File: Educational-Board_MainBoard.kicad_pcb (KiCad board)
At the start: 2 copper layers, 200 x 75 mm, 181 parts, among them J201 Screw_Terminal_01x02_P5mm, J202 USB-C_304A-ACP16X, J401 ACC_INT1, J402 BME_SPI, J403 LUX_INT, J501 RGB_OUT, J601 PWR_IN1, J602 PWR_IN2, J603 PWR_IN3, J604 PWR_IN4, J605 MCP_INT, J606 5V, J607 GND, J608 3V3, J609 EX_PA, J610 EX_PB, J611 PWR_OUT1, J612 PWR_OUT3, J613 PWR_OUT2, J614 PWR_OUT4, Q501 AO3400A, Q601 IRLML9301TRPBF, Q602 IRLML9301TRPBF, Q603 IRLML9301TRPBF, Q604 IRLML9301TRPBF, SW301 RESET, SW501 BUTTON1, SW502 BUTTON2, SW503 BUTTON3, SW504 BUTTON4, SW505 BUTTON5, U201 TPS5430DDA, U202 NUCLEO64-H503RB, U401 LSM6DS3, U402 BME280, U403 OPT4001, U404 INA2180A2, U406 YK16S-L7.2-B10Ka(32-8)-G-A29, U501 74LVC1G34, U502 SSD1315 OLED 0.98", U601 TLP291-4, U602 TLP291-4, U603 MCP23017_SS

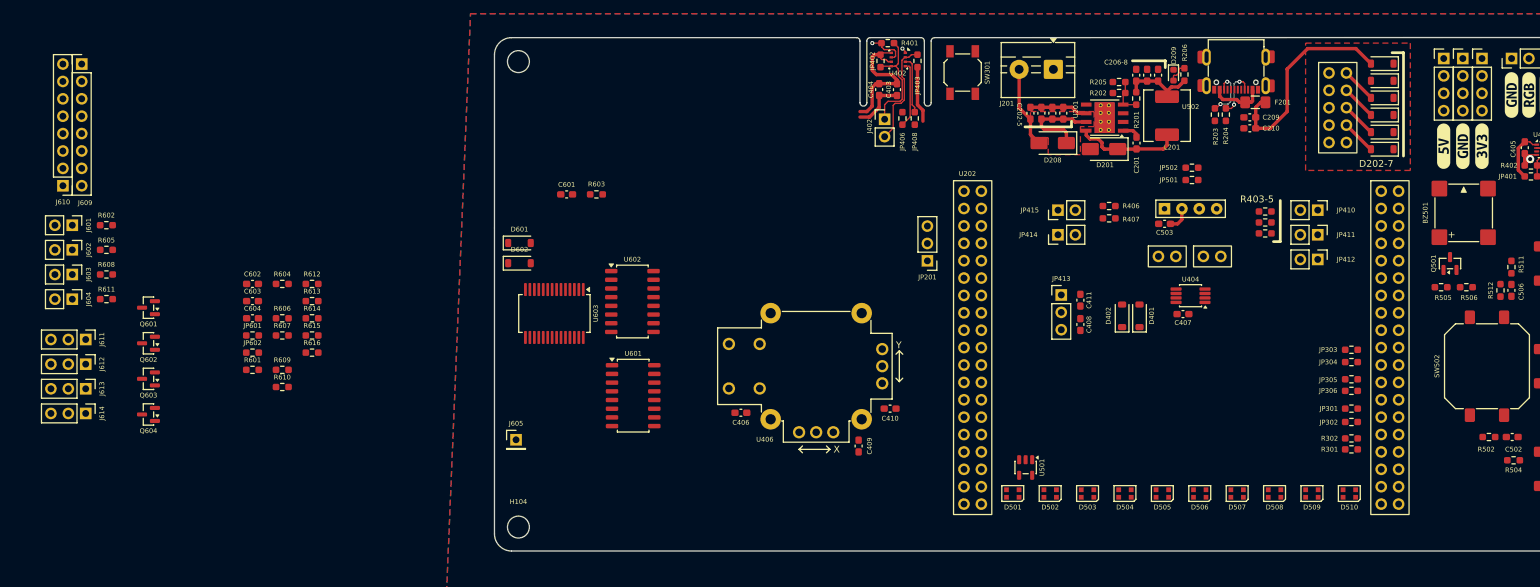
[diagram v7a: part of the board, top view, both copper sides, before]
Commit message: Roued the majority of the nets of the POWER IO
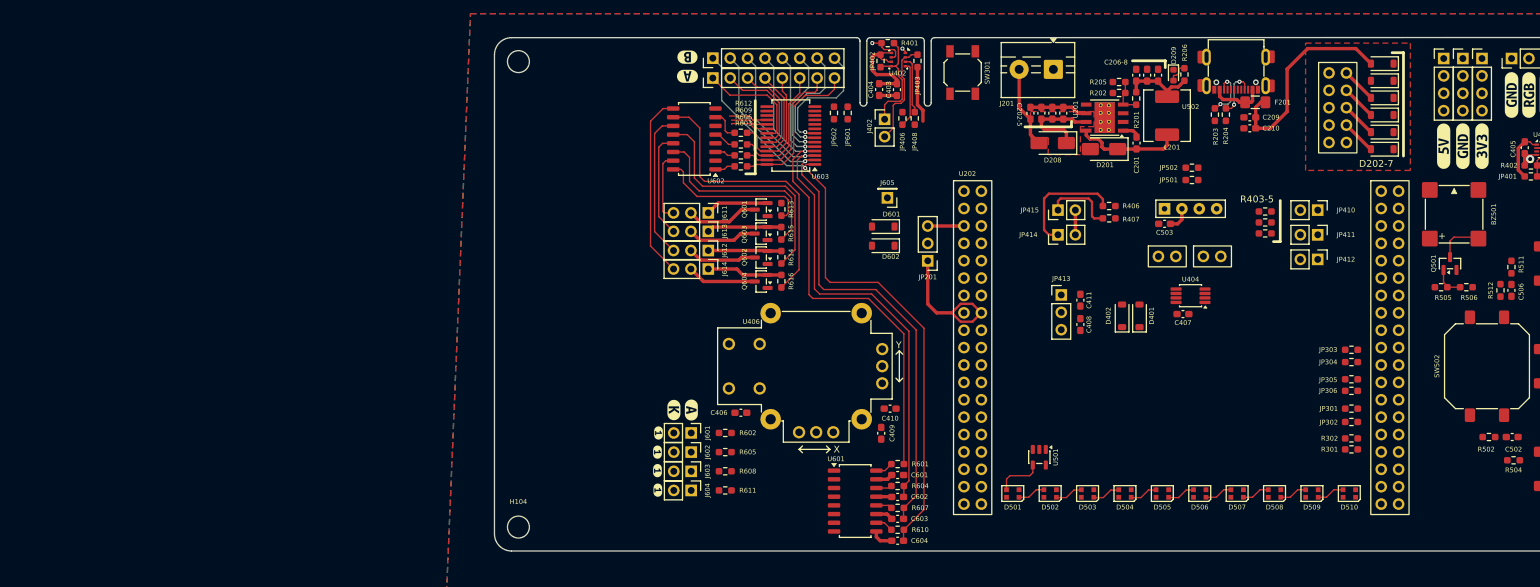
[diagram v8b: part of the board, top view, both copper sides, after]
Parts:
- added kibuzzard-69F28E96: G***, kibuzzard-69F28E96, F.Cu at (78.8, 104.4)
- added kibuzzard-69F28E96: G***, kibuzzard-69F28E96, F.Cu at (78.2, 55.6)
- added kibuzzard-69F28EB1: G***, kibuzzard-69F28EB1, F.Cu at (78.2, 52.9)
- added kibuzzard-69F2951E: G***, kibuzzard-69F2951E, F.Cu at (76.2, 104.4)
- added kibuzzard-69F29536: G***, kibuzzard-69F29536, F.Cu at (73.8, 110.6)
- added kibuzzard-69F29536: G***, kibuzzard-69F29536, F.Cu at (73.8, 113.3)
- added kibuzzard-69F29536: G***, kibuzzard-69F29536, F.Cu at (73.9, 116.1)
- added kibuzzard-69F29536: G***, kibuzzard-69F29536, F.Cu at (74.0, 107.8)
- moved C604 99.7 mm to (108.9, 123.5), turned to 180 degrees
- moved C603 99.5 mm to (108.9, 120.3), turned to 180 degrees
- moved C602 99.3 mm to (108.9, 117.1), turned to 180 degrees
- moved J610 96.8 mm to (81.9, 53.0), turned to 90 degrees
- moved R602 95.4 mm to (83.7, 107.8)
- moved J601 95.4 mm to (78.7, 107.8)
- moved R601 95.3 mm to (108.9, 112.3), turned to 180 degrees
- moved J602 95.1 mm to (78.7, 110.5)
- moved R605 95.1 mm to (83.7, 110.5)
- moved J603 94.9 mm to (78.7, 113.4)
- moved R608 94.9 mm to (83.7, 113.3)
- moved J604 94.6 mm to (78.7, 116.2)
- moved R611 94.6 mm to (83.7, 116.2)
- moved R604 94.6 mm to (108.9, 115.5), turned to 180 degrees
- moved J613 93.8 mm to (81.2, 78.3)
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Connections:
- net Net-(JP410-B) renamed /Sensors/SHUNT_3V3
- net Net-(U202B-VDD_MCU) renamed /Sensors/SHUNT_MCU_VDD
- C601 pad 1: /POWER_UI/PA0 -> /POWER_UI/PB3
- C602 pad 1: /POWER_UI/PA1 -> /POWER_UI/PB2
- C603 pad 1: /POWER_UI/PA2 -> /POWER_UI/PB1
- C604 pad 1: /POWER_UI/PA3 -> /POWER_UI/PB0
- JP414 pad 2: Net-(JP414-B) -> /Sensors/SHUNT_VDD
- JP415 pad 2: Net-(JP414-B) -> /Sensors/SHUNT_VDD
- R403 pad 1: Net-(U202C-VDD) -> /Sensors/SHUNT_VDD
- R404 pad 1: Net-(U202C-VDD) -> /Sensors/SHUNT_VDD
- R405 pad 1: Net-(U202C-VDD) -> /Sensors/SHUNT_VDD
- R601 pad 1: /POWER_UI/PA0 -> /POWER_UI/PB3
- R603 pad 1: /POWER_UI/PA4 -> /POWER_UI/PA7
- R604 pad 1: /POWER_UI/PA1 -> /POWER_UI/PB2
- R606 pad 1: /POWER_UI/PA5 -> /POWER_UI/PA6
- R607 pad 1: /POWER_UI/PA2 -> /POWER_UI/PB1
- R609 pad 1: /POWER_UI/PA6 -> /POWER_UI/PA5
- R610 pad 1: /POWER_UI/PA3 -> /POWER_UI/PB0
- R612 pad 1: /POWER_UI/PA7 -> /POWER_UI/PA4
- U202 pad 78: Net-(JP414-B) -> /Sensors/SHUNT_VDD
- U202 pad 79: Net-(U202C-VDD) -> /Sensors/SHUNT_VDD
- U404 pad 2: Net-(U202C-VDD) -> /Sensors/SHUNT_VDD
- U404 pad 5: Net-(JP414-B) -> /Sensors/SHUNT_VDD
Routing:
- net /POWER_UI/PB0: track 0.00 -> 91.8 mm, vias 0 -> 1
- net /POWER_UI/PB1: track 0.00 -> 87.0 mm, vias 0 -> 1
- net /POWER_UI/PB2: track 0.00 -> 82.5 mm, vias 0 -> 1
- net /POWER_UI/PB3: track 0.00 -> 76.6 mm, vias 0 -> 1
- net /POWER_UI/BJT4_C: track 0.00 -> 41.9 mm
- net /POWER_UI/BJT3_C: track 0.00 -> 35.3 mm
- net /POWER_UI/BJT2_C: track 0.00 -> 28.8 mm
- net /POWER_UI/BJT4_GND: track 0.00 -> 27.1 mm
- net /POWER_UI/PA7: track 0.00 -> 23.0 mm
- net /POWER_UI/BJT1_C: track 0.00 -> 22.7 mm
- net /POWER_UI/BJT3_GND: track 0.00 -> 21.4 mm
- net /MCU/NUCLEO_3V3: track 0.00 -> 21.2 mm
- net /POWER_UI/PA6: track 0.00 -> 20.3 mm
- net /POWER_UI/PB7: track 0.00 -> 18.9 mm, vias 0 -> 1
- net /POWER_UI/PA5: track 0.00 -> 18.2 mm
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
